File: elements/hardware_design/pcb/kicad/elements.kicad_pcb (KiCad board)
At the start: 2 copper layers, 164.5 x 106 mm, 196 parts, among them IC1 LM4040B10, IC10 STM32F405RGT6, IC11 4051PW, IC13 MCP6004, IC14 TL072, IC2 LM1117-3.3, IC3 4051PW, IC4 LM1117-3.3, IC5 4051PW, IC6 MCP6004, IC7 MCP6004, IC8 4051PW, IC9 MCP6002, J1 PJ301_THONKICONN6, J10 PJ301_THONKICONN6, J11 PJ301_THONKICONN6, J12 PJ301_THONKICONN6, J13 PJ301_THONKICONN6, J14 PJ301_THONKICONN6, J15 PJ301_THONKICONN6, J16 PJ301_THONKICONN6, J17 PJ301_THONKICONN6, J18 PJ301_THONKICONN6, J2 PJ301_THONKICONN6, J3 PJ301_THONKICONN6, J4 PJ301_THONKICONN6, J5 PJ301_THONKICONN6, J6 PJ301_THONKICONN6, J7 PJ301_THONKICONN6, J8 PJ301_THONKICONN6, J9 PJ301_THONKICONN6, Q1 8MHz, Q2 MMBT3904, SW1 SW_MEC_5G_2LED, SW2 EVQQ2, SW3 EVQQ2, U1 WM8731CLSEFL

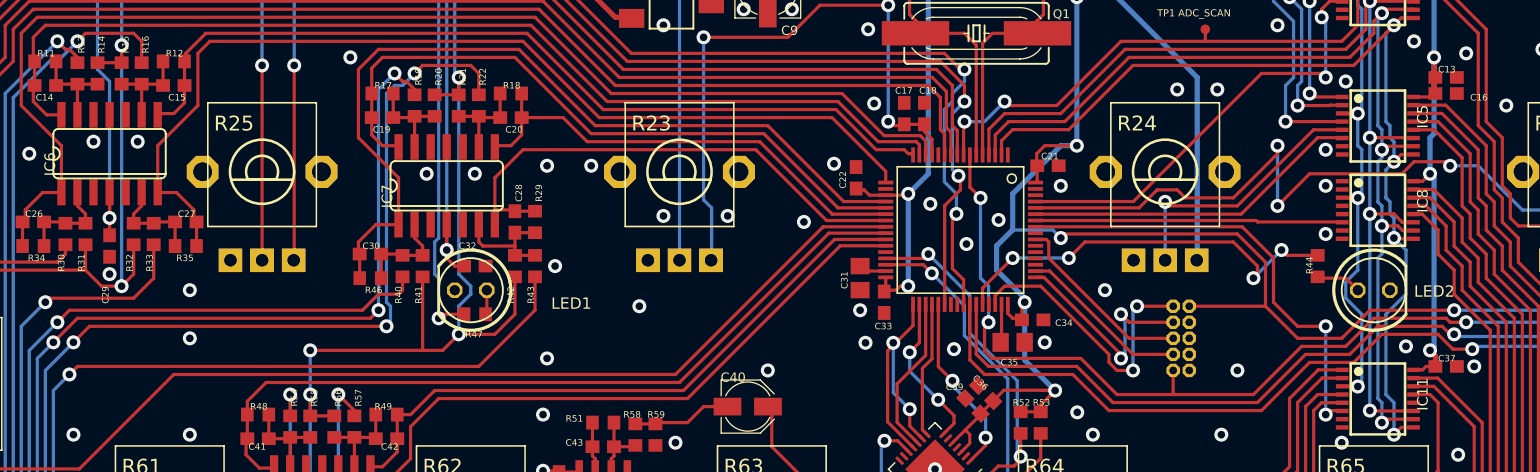
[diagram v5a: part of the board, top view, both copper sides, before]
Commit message: SMD LEDs
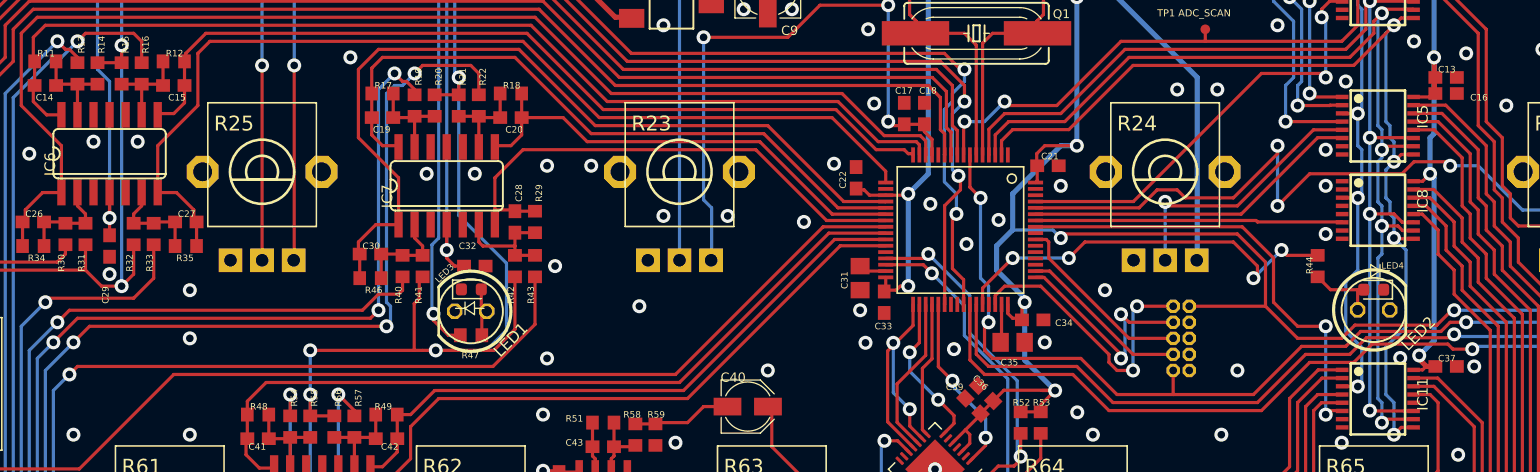
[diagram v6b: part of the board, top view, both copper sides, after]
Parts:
- added LED3: SSL-LX5093TC, LED_SMD:LED_0603_1608Metric, F.Cu at (126.3, 98.3)
- added LED4: SSL-LX5093PC, LED_SMD:LED_0603_1608Metric, F.Cu at (197.7, 98.3)
- moved R47 1.68 mm to (126.3, 101.9)
- moved LED1 1.66 mm to (126.3, 100.0)
- moved LED2 1.56 mm to (197.7, 99.9)
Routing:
- net AREF_-10: track 198.7 -> 206.4 mm
- net Net-(LED2-PadA): track 3.61 -> 5.68 mm
- net Net-(LED1-PadA): track 1.95 -> 3.97 mm
- net +3V3_A: track 890.8 -> 892.0 mm
- net Net-(IC10-Pad41): track 94.6 -> 95.3 mm
- net Net-(J15-PadP3): track 177.0 -> 177.7 mm
- net /elements_2/TX: track 85.6 -> 85.0 mm
- net /elements_2/RX: track 86.0 -> 85.5 mm

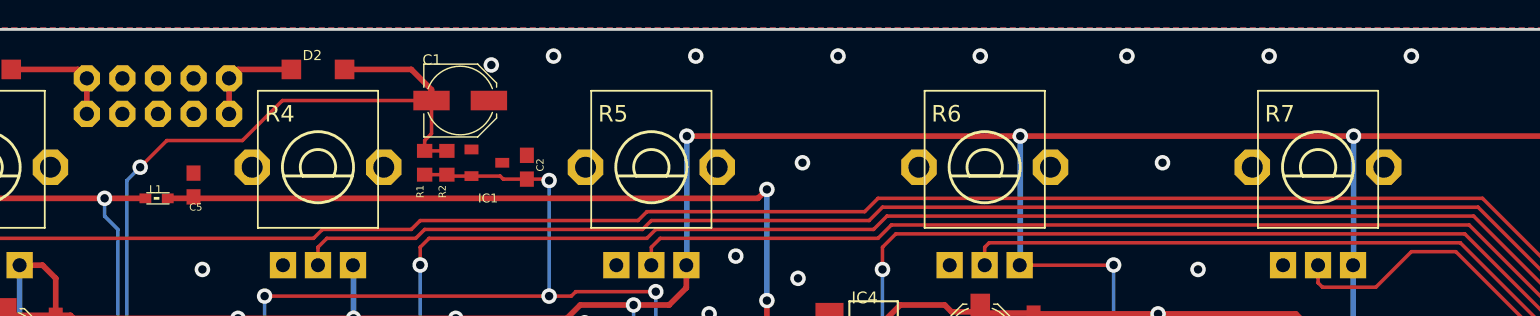
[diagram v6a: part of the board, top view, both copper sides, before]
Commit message: add optional SMD power
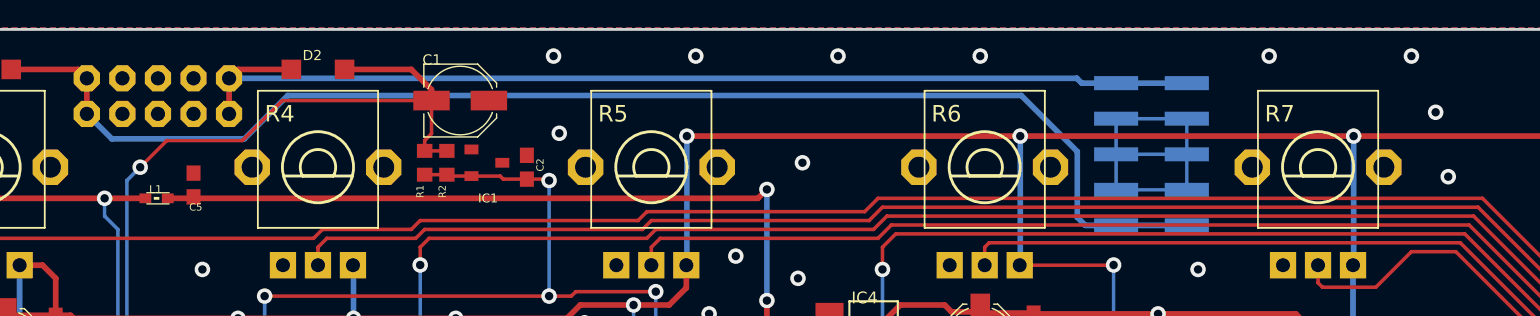
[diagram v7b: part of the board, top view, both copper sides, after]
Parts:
- added J19: Conn_02x05_Odd_Even, Connector_PinHeader_2.54mm:PinHeader_2x05_P2.54mm_Vertical_SMD, B.Cu at (162.0, 60.9)
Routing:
- net Net-(D1-PadA): track 8.21 -> 95.4 mm
- net Net-(D2-PadC): track 7.25 -> 75.8 mm
- net GND: track 3.32 -> 28.6 mm
